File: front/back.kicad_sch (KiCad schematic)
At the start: 1 part, among them U4 PCA9615DP

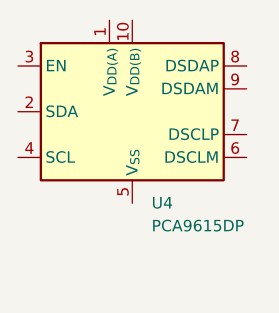
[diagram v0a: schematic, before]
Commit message: add some traces
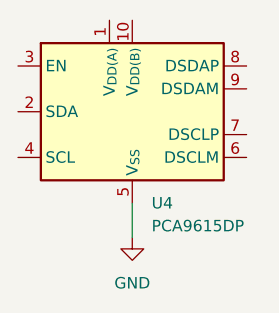
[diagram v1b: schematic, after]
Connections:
- net GND: now reaches U4.5 (V_{SS})
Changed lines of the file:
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@@
 	(generator_version "9.0")
 	(paper "A4")
+	(wire
+		(pts
+			(xy 142.24 83.82) (xy 142.24 87.63)
+		)
+		(stroke
+			(width 0)
+			(type default)
+		)
+	)
 	(symbol
 		(lib_id "Interface:PCA9615DP")
@@
 					(unit 1)
 				)
+			)
+		)
+	)
+	(symbol
+		(lib_id "power:GND")
+		(at 142.24 87.63 0)
+		(unit 1)
+		(exclude_from_sim no)
+		(in_bom yes)
+		(on_board yes)
+		(dnp no)
+		(fields_autoplaced yes)
+		(property "Reference" "#PWR04"
+			(at 142.24 93.98 0)
+			(effects
+				(font
+					(size 1.27 1.27)
+				)
+				(hide yes)
+			)
+		)
+		(property "Value" "GND"
+			(at 142.24 92.71 0)
+			(effects
+				(font
+					(size 1.27 1.27)
+				)
+			)
+		)
+		(property "Footprint" ""
+			(at 142.24 87.63 0)
+			(effects
+				(font
+					(size 1.27 1.27)
+				)
+				(hide yes)
+			)
+		)
+		(property "Datasheet" ""
+			(at 142.24 87.63 0)
+			(effects
+				(font
+					(size 1.27 1.27)
+				)
+				(hide yes)
+			)
+		)
+		(property "Description" "Power symbol creates a global label with name \"GND\" , ground"
+			(at 142.24 87.63 0)
+			(effects
+				(font
+					(size 1.27 1.27)
+				)
+				(hide yes)
+			)
+		)
+		(pin "1"
+		)
+		(instances
+			(project ""
+				(path "/508f986b-6f1b-4c39-bd57-bae69573a4e7/7930c339-f26f-415c-a8d1-ea724abb9afc"
+					(reference "#PWR04")
+					(unit 1)
+				)

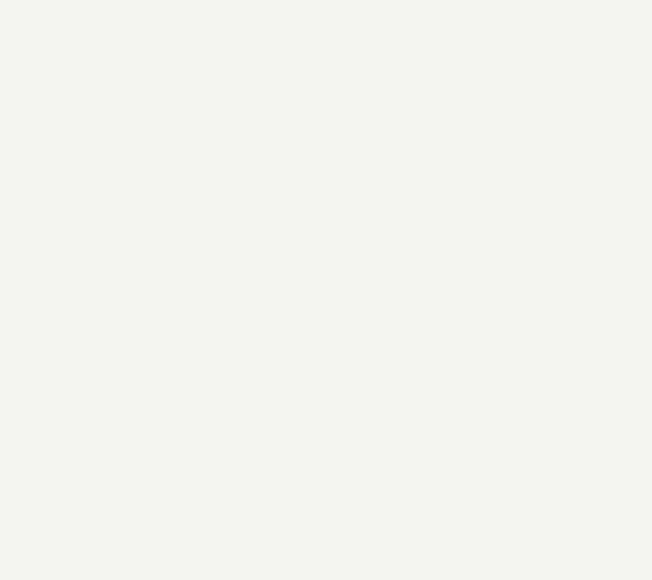
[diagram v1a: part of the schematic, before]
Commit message: undo panelizing
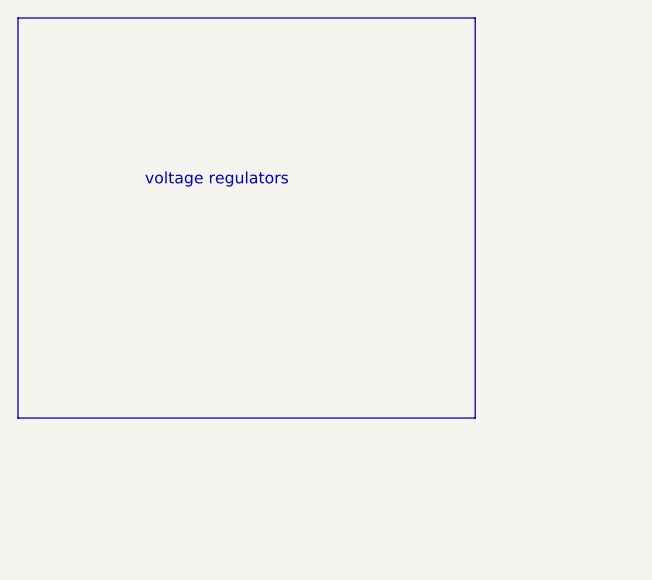
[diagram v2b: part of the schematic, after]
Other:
- note added: "voltage regulators"
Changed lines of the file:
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@@
 	(generator_version "9.0")
 	(paper "A4")
+	(rectangle
+		(start 43.18 31.75)
+		(end 93.98 76.2)
+		(stroke
+			(width 0)
+			(type default)
+		)
+		(fill
+			(type none)
+		)
+	)
+	(text "voltage regulators\n"
+		(exclude_from_sim no)
+		(at 65.278 49.784 0)
+		(effects
+			(font
+				(size 1.27 1.27)
+			)
+		)
+	)
 	(wire
 		(pts

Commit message: begin layout
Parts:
- added C10, C6, C7: 100n, Capacitor_SMD:C_0603_1608Metric, symbol Device:C
- added C11: 1u, Capacitor_SMD:C_0603_1608Metric, symbol Device:C
- added C12: 10n, Capacitor_SMD:C_0402_1005Metric, symbol Device:C
- added C13: 4.7u, Capacitor_SMD:C_0603_1608Metric, symbol Device:C
- added C14, C9: 22u, Capacitor_SMD:C_0805_2012Metric, symbol Device:C
- added C8: 10u, Capacitor_SMD:C_0805_2012Metric, symbol Device:C
- added J6: Conn_01x06_Pin, Connector_PinHeader_2.54mm:PinHeader_1x06_P2.54mm_Horizontal, symbol Connector:Conn_01x06_Pin
- added L1: 2.2u, Inductor_SMD:L_Vishay_IHLP-3232, symbol Device:L
- added L2: 1u, Library:INDC2520X120N, symbol New_Library:DFE252012F-1R0M=P2
- added NT3: NetTie_3, Jumper:SolderJumper-3_P1.3mm_Bridged12_RoundedPad1.0x1.5mm, symbol Device:NetTie_3
- added R10: 200k, Resistor_SMD:R_0603_1608Metric, symbol Device:R
- added R11: 100k, Resistor_SMD:R_0603_1608Metric, symbol Device:R
- added R8: 61.9k, Resistor_SMD:R_0603_1608Metric, symbol Device:R
- added R9: 249k, Resistor_SMD:R_0603_1608Metric, symbol Device:R
- added U1: LSM6DSO32TR, Library:XDCR_LSM6DSO32TR, symbol New_Library:LSM6DSO32TR
- added U5: TPS62902RPJR, Library:IC_TPS62902RPJR, symbol New_Library:TPS62902RPJR
- added U6: TLV62568ADRL, Package_TO_SOT_SMD:SOT-563, symbol Regulator_Switching:TLV62568ADRL
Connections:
- net GND: now also C10.2, C11.2, C12.2, C13.2, C14.2, C6.2, C7.2, C8.2, C9.2, J6.3 (Pin_3), J6.4 (Pin_4), NT3.1, R11.2, R8.2, R9.2, U1.2 (SDX), U1.3 (SCX), U1.6 (GND), U1.7 (GND__1), U5.1 (PG), U5.4 (GND), U6.2 (GND)
- net 3.3v: now reaches U4.1 (V_{DD(A)})
- net 3.3v: now also U4.10 (V_{DD(B)}), C10.1, C11.1, C13.1, C6.1, C7.1, C9.1, J6.2 (Pin_2), L1.2, U1.12 (CS), U1.5 (VDDIO), U1.8 (VDD), U5.3 (VOS), U6.3 (VIN), U6.5 (EN)
- net sdimu: now reaches U4.2 (SDA)
- net sdimu: now also J6.6 (Pin_6), U1.14 (SDA)
- net scimu: now reaches U4.4 (SCL)
- net scimu: now also J6.5 (Pin_5), U1.13 (SCL)
- new net: L2.1, U6.4 (SW)
- new net: L1.1, U5.2 (SW)
- new net: R10.2, R11.1, U6.1 (FB)
- new net: C12.1, U5.7 (MODE/S-CONF)
- new net: R8.1, U5.8 (SS/TR)
- new net: R9.1, U5.9 (FB/VSET)
- new net: NT3.2, U1.1 (SDO/SA0)
- new net 1.8v: C14.1, J6.1 (Pin_1), L2.2, NT3.3, R10.1
- new net bat+: C8.1, U5.5 (EN), U5.6 (VIN)
- no-connect marks 0 -> 3
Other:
- note removed: "voltage regulators"
- moved on the sheet: U4

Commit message: push changes
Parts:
- added J7: Conn_01x08_Pin, Library:JST_XH_B8B-XH-AM_1x08_P2.50mm_Vertical, symbol Connector:Conn_01x08_Pin
- C10: value 100n -> 1u
- C11: value 1u -> 100n
- C12: footprint Capacitor_SMD:C_0402_1005Metric -> Capacitor_SMD:C_0603_1608Metric; Mfr PN (none) -> GRM1857U1A103JA44D
- C8: Mfr PN (none) -> MSAST21GBB5106MTNA01
- L1: footprint Inductor_SMD:L_Vishay_IHLP-3232 -> Library:WE-XHMI_4020; Mfr (none) -> Würth Elektronik; Mfr PN IHLP3232DZER2R2M11 -> 74439323022; Supplier (none) -> digikey.com; Supplier PN (none) -> 732-74439323022CT-ND
- R8: Mfr PN (none) -> CRCW060361K9FKEA
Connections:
- net 3.3v: now also J6.4 (Pin_4); no longer J6.2 (Pin_2)
- net GND: now also J6.5 (Pin_5), J6.6 (Pin_6), J7.5 (Pin_5), J7.6 (Pin_6); no longer J6.3 (Pin_3), J6.4 (Pin_4)
- net bat+: now also J7.7 (Pin_7), J7.8 (Pin_8)
- net scimu: now also J6.2 (Pin_2); no longer J6.5 (Pin_5)
- net sdimu: now also J6.3 (Pin_3); no longer J6.6 (Pin_6)
- net at U4.6 (DSCLM): now also J7.4 (Pin_4)
- net at U4.7 (DSCLP): now also J7.3 (Pin_3)
- net at U4.8 (DSDAP): now also J7.2 (Pin_2)
- net at U4.9 (DSDAM): now also J7.1 (Pin_1)
- net at U5.7 (MODE/S-CONF): now also R8.1; no longer C12.1
- net at U5.8 (SS/TR): now also C12.1; no longer R8.1
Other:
- note added: "https://webench.ti.com/appinfo/webench/scripts/SDP.cgi?ID=64526E0ADC16EFE7"
- moved on the sheet: C10, C11, C13
